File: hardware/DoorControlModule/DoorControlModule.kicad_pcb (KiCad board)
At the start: 6 copper layers, 68.8 x 65 mm, 135 parts, among them IC1 CY8C4147AZE-S475, IC2 TLS850B0TBV50ATMA1, IC3 TJA1043T,118, IC4 MAX6818, IC5 LM2901BYPT, IC6 BTS72002EPAXUMA1, IC7 LM74610, J1 501331-0507, J2 64334-0100, Q1 VOMA618A-4X001T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

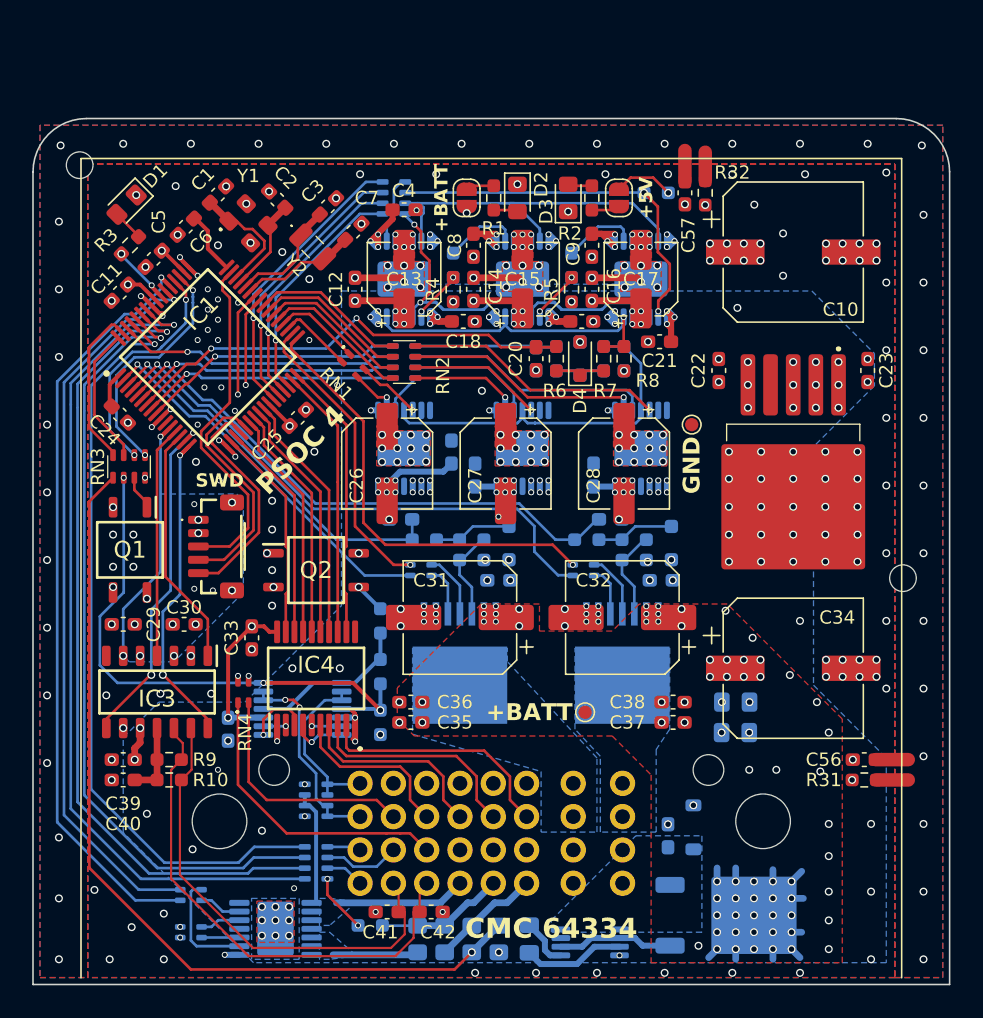
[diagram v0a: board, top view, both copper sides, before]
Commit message: comparator routing updated
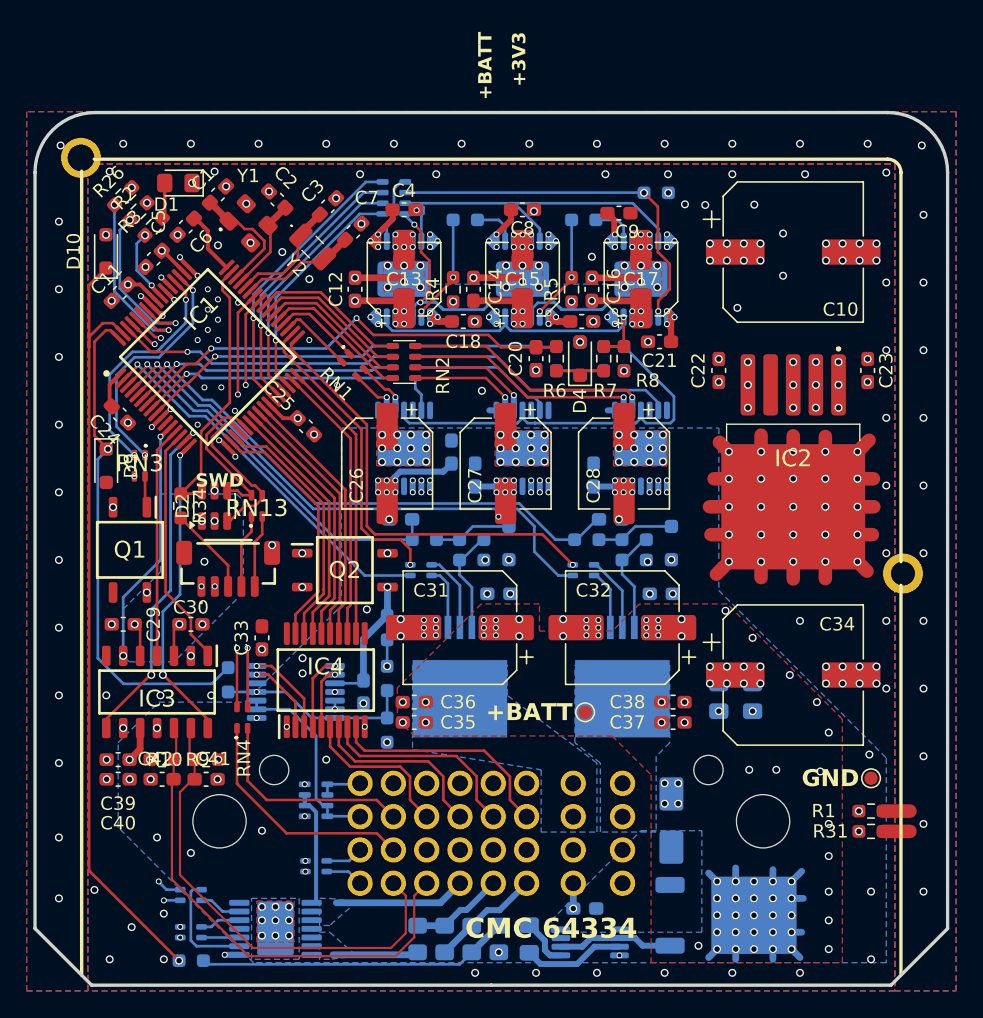
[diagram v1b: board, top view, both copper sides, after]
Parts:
- removed C56, C57: 100p, Capacitor_SMD:C_0603_1608Metric_Pad1.08x0.95mm_HandSolder
- removed D8: 33V TVS, Diode_SMD:D_SOD-123
- removed JP1, JP2: SolderJumper_2_Open, Jumper:SolderJumper-2_P1.3mm_Open_RoundedPad1.0x1.5mm
- removed RN10: 2k0, SamacSys:CAY1647R0F4LF
- added D10: 3V Z, Diode_SMD:D_SOD-323_HandSoldering, F.Cu at (107.9, 61.7)
- added D9: 3V Z, Diode_SMD:D_SOD-323_HandSoldering, F.Cu at (108.0, 77.8)
- added R33: 2k2, Resistor_SMD:R_0603_1608Metric_Pad0.98x0.95mm_HandSolder, B.Cu at (114.3, 114.9)
- added R34: 2k, Resistor_SMD:R_0603_1608Metric_Pad0.98x0.95mm_HandSolder, F.Cu at (113.5, 80.8)
- added RN13: 2k0, SamacSys:CAY16220J2LF, F.Cu at (119.3, 80.8)
- added RN14: 2k0, SamacSys:CAY16220J2LF, B.Cu at (123.7, 107.8)
- D2: value LED -> ESDA6V1BC6; footprint LED_SMD:LED_0805_2012Metric_Pad1.15x1.40mm_HandSolder -> Package_TO_SOT_SMD:SOT-23-6
- D3: value LED -> SMAJ28A; footprint LED_SMD:LED_0805_2012Metric_Pad1.15x1.40mm_HandSolder -> Diode_SMD:D_SMA; moved to B.Cu
- IC2: value TLS850B0TBV50ATMA1 -> TLS850B0TBV33ATMA1
- J2: footprint SamacSys:643340100 -> SamacSys:64334_JO32_2
- R1: value 2k2 -> 10R
- R10, R9: value 60R -> 2k
- R11, R3, R4, R5: value 1k0 -> 1k2
- R2: value 1k0 -> DNP
- R26: moved to F.Cu
- R32: value 10R -> 2k2; moved to B.Cu
- RN3: footprint SamacSys:CAY1647R0F4LF -> SamacSys:CAY16220J2LF
- U3, U4, U5: value BTN7030_1EPA -> BTN70301EPAXUMA1
- moved R26 57.8 mm to (109.2, 57.5), turned to 45 degrees
- moved R1 54.0 mm to (165.4, 103.7), turned to 180 degrees
- moved R32 51.2 mm to (117.1, 93.8), turned to 90 degrees
- moved D3 47.4 mm to (150.4, 104.4)
- moved R2 34.1 mm to (110.4, 58.7), turned to 45 degrees
- moved D2 32.4 mm to (116.1, 80.8), turned to 90 degrees
- moved TP2 29.8 mm to (165.4, 101.2)
- moved J2 28.7 mm to (102.6, 116.8)
- moved C42 22.5 mm to (112.1, 101.3), turned to 0 degrees
- moved C41 16.8 mm to (115.4, 101.3), turned to 0 degrees
- moved C53 10.5 mm to (127.3, 94.7)
- moved C54 8.30 mm to (143.9, 111.0), turned to 180 degrees
- moved C8 4.55 mm to (139.2, 58.5), turned to 0 degrees
- moved D1 4.21 mm to (113.4, 56.5), turned to 180 degrees
- moved R31 3.89 mm to (165.4, 105.2)
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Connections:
- C33 pad 1: VDD_COMP -> VDD_DEB
- C53 pad 1: VDD_COMP -> VCC_COMP
- D2 pad 1: GND -> VDD
- D2 pad 2: Net-(D2-A) -> GND
- D3 pad 1: GND -> VBAT
- D3 pad 2: Net-(D3-A) -> GND
- IC1 pad 18: PWS_RIGHT_DOWN_DEB -> PWS_RIGHT_LOCK_UP_DEB
- IC1 pad 19: PWS_RIGHT_LOCK_DOWN_DEB -> PWS_RIGHT_UP_DEB
- IC1 pad 22: PWS_RIGHT_UP_DEB -> PWS_RIGHT_LOCK_DOWN_DEB
- IC1 pad 23: PWS_RIGHT_LOCK_UP_DEB -> PWS_RIGHT_DOWN_DEB
- IC1 pad 58: DIO_4 -> ID_2
- IC1 pad 59: DIO_3 -> ID_1
- IC4 pad 16: PWS_RIGHT_LOCK_UP_DEB -> PWS_RIGHT_DOWN_DEB
- IC4 pad 17: PWS_RIGHT_UP_DEB -> PWS_RIGHT_LOCK_DOWN_DEB
- IC4 pad 18: PWS_RIGHT_LOCK_DOWN_DEB -> PWS_RIGHT_UP_DEB
- IC4 pad 19: PWS_RIGHT_DOWN_DEB -> PWS_RIGHT_LOCK_UP_DEB
- IC4 pad 2: PWS_RIGHT_DOWN -> PWS_RIGHT_LOCK_UP
- IC4 pad 20: VDD_COMP -> VDD_DEB
- IC4 pad 3: PWS_RIGHT_LOCK_DOWN -> PWS_RIGHT_UP
- IC4 pad 4: PWS_RIGHT_UP -> PWS_RIGHT_LOCK_DOWN
- IC4 pad 5: PWS_RIGHT_LOCK_UP -> PWS_RIGHT_DOWN
- IC5 pad 3: VDD_COMP -> VCC_COMP
- J1 pad 3: XRES -> Net-(J1-Pad3)
- J1 pad 4: SWD_CLK -> Net-(J1-Pad4)
- J1 pad 5: SWD_DATA -> Net-(J1-Pad5)
- J1 pad 6: VDD -> GND
- J1 pad 7: VDD -> GND
- J2 pad A1: power_window_switch_up_right -> power_window_switch_down_right
- J2 pad A2: power_window_switch_down_right -> power_window_switch_up_right
- J2 pad A4: digital_io_3 -> digital_io_2
- J2 pad B3: digital_io_2 -> door_lock_sensor_locking
- J2 pad C3: door_lock_sensor_locking -> GND
- Q1 pad 1: EN_2_ -> EN_1_
- Q1 pad 3: VDD_COMP -> VDD_DEB
- Q2 pad 1: EN_1_ -> EN_2_
- R1 pad 1: Net-(JP1-A) -> Earth
- R1 pad 2: Net-(D2-A) -> GND
- R2 pad 1: Net-(JP2-A) -> ID_2
- R2 pad 2: Net-(D3-A) -> GND
- R26 pad 1: DIO_4_ -> ID_1
- R26 pad 2: variable_resistor_high -> GND
- R32 pad 1: Earth -> AI_6_
- R32 pad 2: GND -> AI_6
- RN3 pad 3: AI_6 -> EN_2_
- RN3 pad 4: AI_5 -> EN_1_
- RN9 pad 5: power_window_switch_up_right -> power_window_switch_down_right
- RN9 pad 6: power_window_switch_up_right -> power_window_switch_down_right
- RN9 pad 7: power_window_switch_down_right -> power_window_switch_up_right
- RN9 pad 8: power_window_switch_down_right -> power_window_switch_up_right
- U3 pad 1: GND -> unconnected-(U3-NC_1-Pad1)
- U3 pad 3: HB_2_IN_ -> HB_2_DEN_
- U3 pad 5: HB_2_DEN_ -> unconnected-(U3-NC_2-Pad5)
- U3 pad 6: unconnected-(U3-NC1-Pad6) -> HB_2_IN_
- U4 pad 1: GND -> unconnected-(U4-NC_1-Pad1)
- U4 pad 3: HB_1_IN_ -> HB_1_DEN_
- U4 pad 5: HB_1_DEN_ -> unconnected-(U4-NC_2-Pad5)
- U4 pad 6: unconnected-(U4-NC1-Pad6) -> HB_1_IN_
- U5 pad 1: GND -> unconnected-(U5-NC_1-Pad1)
- U5 pad 3: MM_IN_ -> MM_DEN_
- U5 pad 5: MM_DEN_ -> unconnected-(U5-NC_2-Pad5)
- U5 pad 6: unconnected-(U5-NC1-Pad6) -> MM_IN_
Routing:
- net DIO_4: track 63.8 -> 0.00 mm, vias 1 -> 0
- net DIO_3: track 61.6 -> 0.00 mm, vias 1 -> 0
- net AI_5: track 12.4 -> 59.4 mm, vias 0 -> 1
- net AI_5_: track 65.3 -> 23.5 mm, vias 1 -> 0
- net AI_6: track 10.4 -> 38.0 mm, vias 0 -> 1
- net AI_6_: track 42.2 -> 14.8 mm, vias 3 -> 1
- net VDD_COMP: track 24.0 -> 0.00 mm, vias 3 -> 0
- net ID_1: track 0.00 -> 14.4 mm, vias 0 -> 2
- net GND: track 38.9 -> 53.2 mm, vias 272 -> 263
- net EN_2_: track 2.60 -> 16.8 mm, vias 0 -> 2
- net ID_2: track 0.00 -> 13.3 mm, vias 0 -> 2
- net power_window_switch_down_right: track 15.4 -> 3.93 mm, vias 2 -> 1
- net EN_1_: track 13.2 -> 2.37 mm, vias 2 -> 0
- net Net-(IC3-SPLIT): track 5.57 -> 14.7 mm, vias 0 -> 4
- net VCC_COMP: track 2.30 -> 10.5 mm
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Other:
- board size 68.8 x 65 mm -> 68.5 x 65.5 mm
- board text added: "+3V3"
- board text added: "Rev.B - MM/YYYY"
- board text removed: "+5V"
- board text removed: "Rev.A - 10/2025"
